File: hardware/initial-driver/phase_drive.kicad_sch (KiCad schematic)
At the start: 71 parts, among them Q1 UFET, Q2 VFET, Q3 WFET, U4 PT5616A, U5 OP07, U6 OP07, U7 OP07, U8 OP07

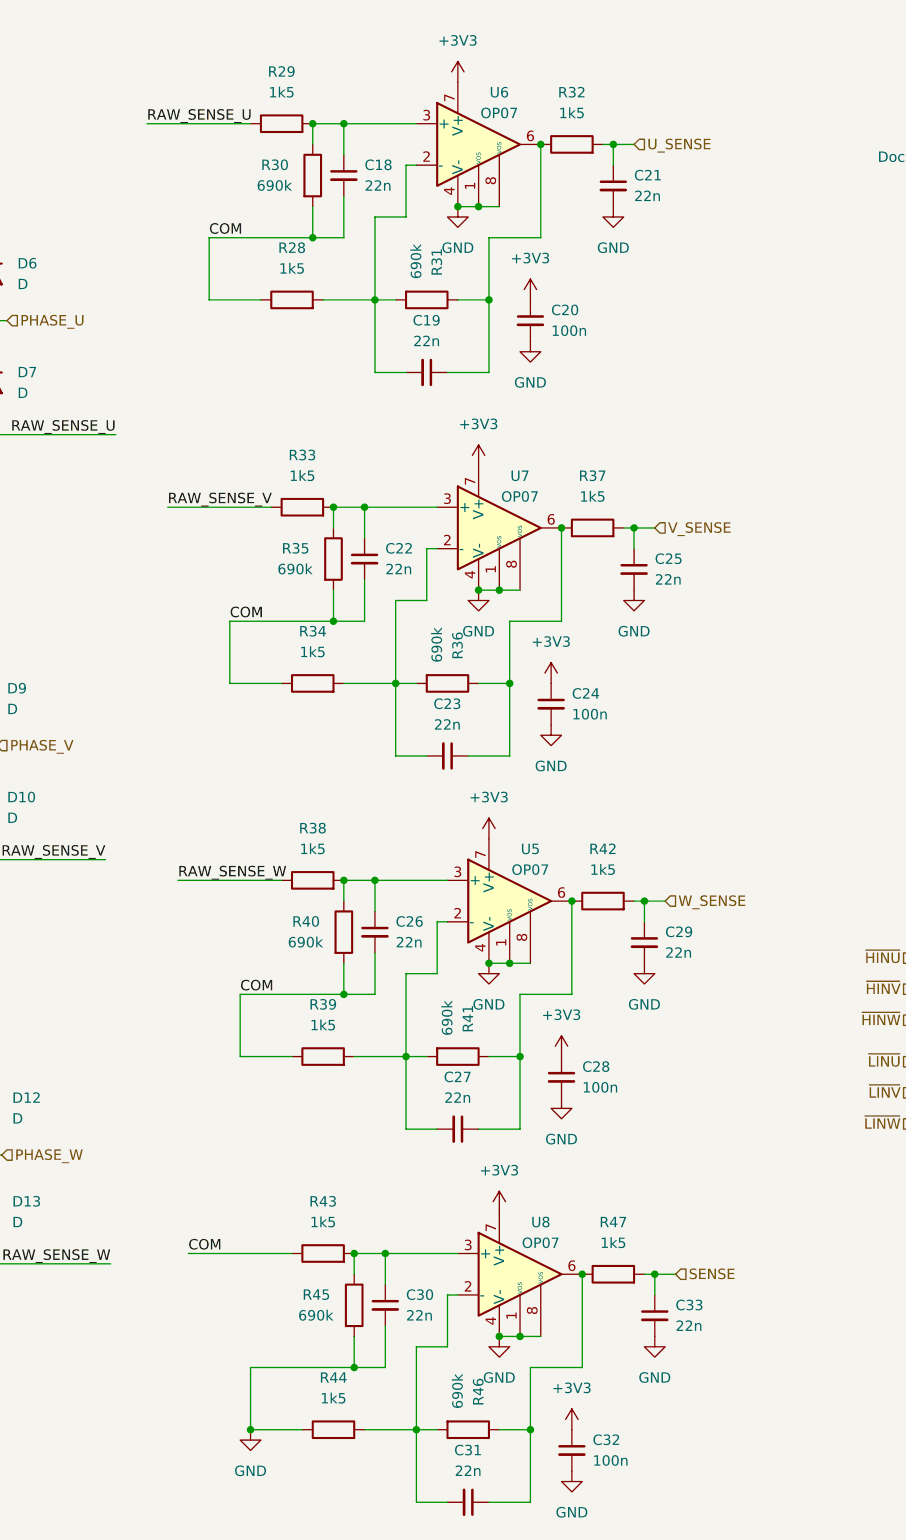
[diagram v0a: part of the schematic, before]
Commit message: Refactor current sensing
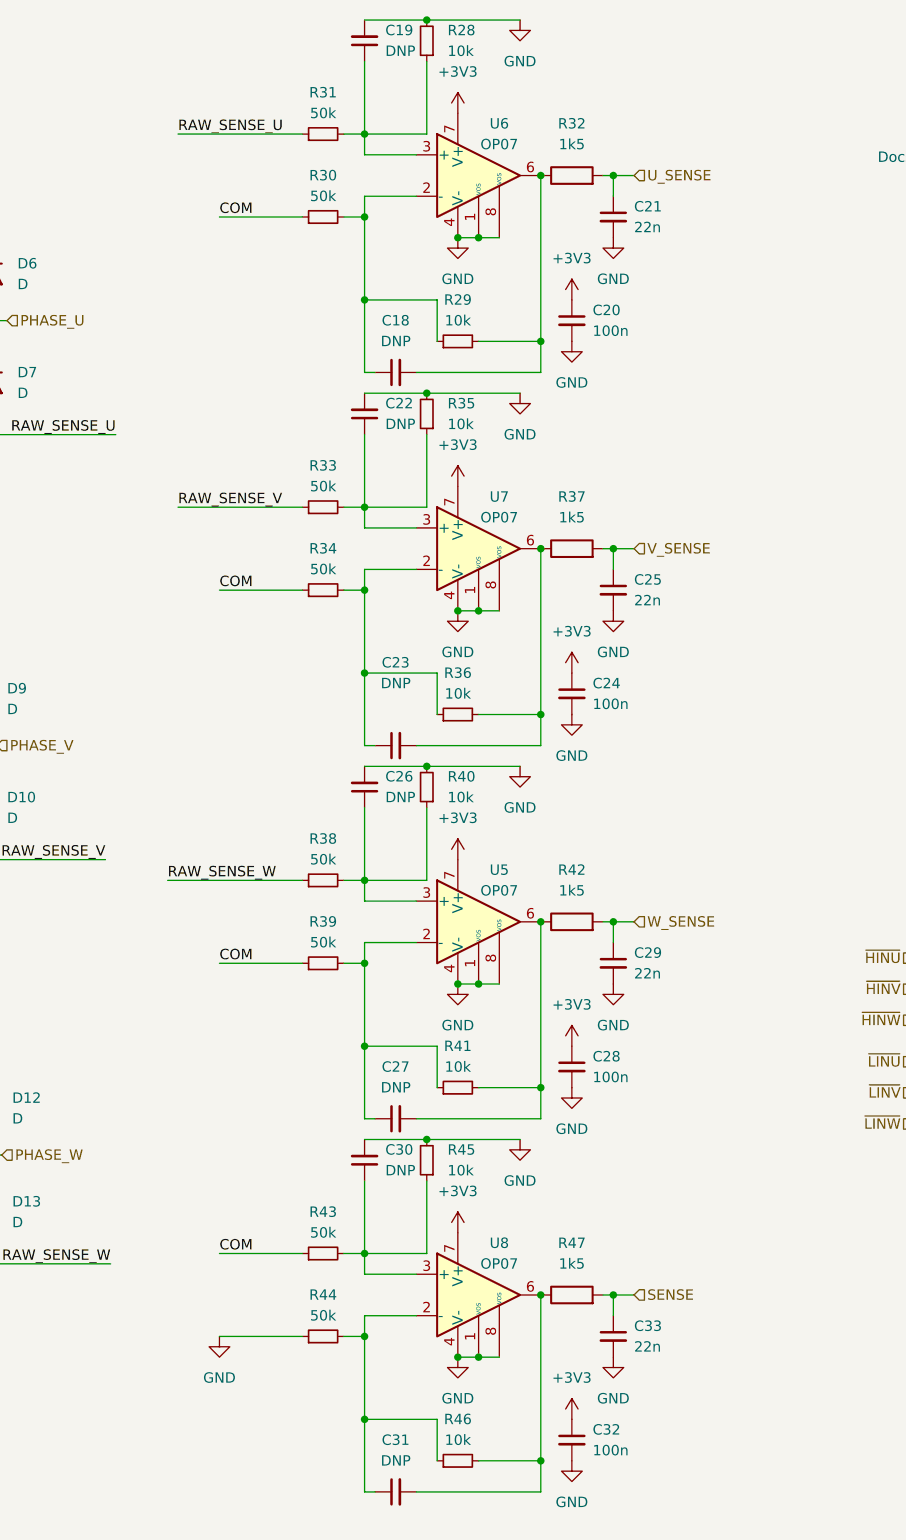
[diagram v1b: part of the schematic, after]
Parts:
- removed R28, R29, R33, R34, R38, R39, R43, R44: 1k5, symbol Device:R
- removed R30, R31, R35, R36, R40, R41, R45, R46: 690k, symbol Device:R
- added R28, R29, R35, R36, R40, R41, R45, R46: 10k, symbol Device:R_Small
- added R30, R31, R33, R34, R38, R39, R43, R44: 50k, symbol Device:R_Small
- C18, C19, C22, C23, C26, C27, C30, C31: value 22n -> DNP
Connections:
- net COM: now also R30.1, R34.1, R39.1, R43.1; no longer C18.2, C22.2, C26.2
- net GND: now also C19.2, C22.2, C26.2, R28.2, R35.2, R40.2, R44.1, R45.2
- net RAW_SENSE_U: now also R31.1
- net RAW_SENSE_V: now also R33.1
- net RAW_SENSE_W: now also R38.1
- net at C27.2: now also R42.1, U5.6, R41.2; no longer U5.2 (-)
- net at C26.1, U5.3 (+): now also R38.2, R40.1
- net at U7.2 (-): now also C23.1, R34.2, R36.1; no longer C23.2
- net at C22.1, U7.3 (+): now also R33.2, R35.1
- net at R37.1, U7.6: now also C23.2, R36.2; no longer C23.1
- net at R32.1, U6.6: now also C18.2, R29.2; no longer C19.1
- net at C30.1, U8.3 (+): now also R43.2, R45.1
- net at U8.2 (-): now also C31.1, R44.2, R46.1; no longer C31.2
- net at R47.1, U8.6: now also C31.2, R46.2; no longer C31.1
- net at U6.2 (-): now also C18.1, R29.1, R30.2; no longer C19.2
- net at U6.3 (+): now also C19.1, R28.1, R31.2; no longer C18.1
- new net: C27.1, R39.2, R41.1, U5.2 (-)
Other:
- moved on the sheet: C20, C21, R32, U6

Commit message: add more stuff
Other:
- note added: "Negative voltage for op amp? Circulating voltage may be an issue"
